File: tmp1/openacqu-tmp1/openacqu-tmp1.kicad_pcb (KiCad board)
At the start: 4 copper layers, 45 x 36 mm, 35 parts, among them J1 GSB1C41110SSHR, J2 Test Points, U1 MCP2221AT-I_ML, U2 LP5817DRLR, U3 FXL6408UMX, U4 24AA025E48T-E_OT, U5 AP2112K-3.3TRG1, U6 TPS22996HQDYCRQ1

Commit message: Added sensor to tmp1
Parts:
- added J3: SJ-3524-SMT, openacqu_footprints:CUI_SJ-3524-SMT, F.Cu at (111.9, 75.0)
- added U7: MCP9600T-E_MX, openacqu_footprints:QFN65P500X500X100-21N_MCP9600T-E_MX, F.Cu at (101.0, 64.2)

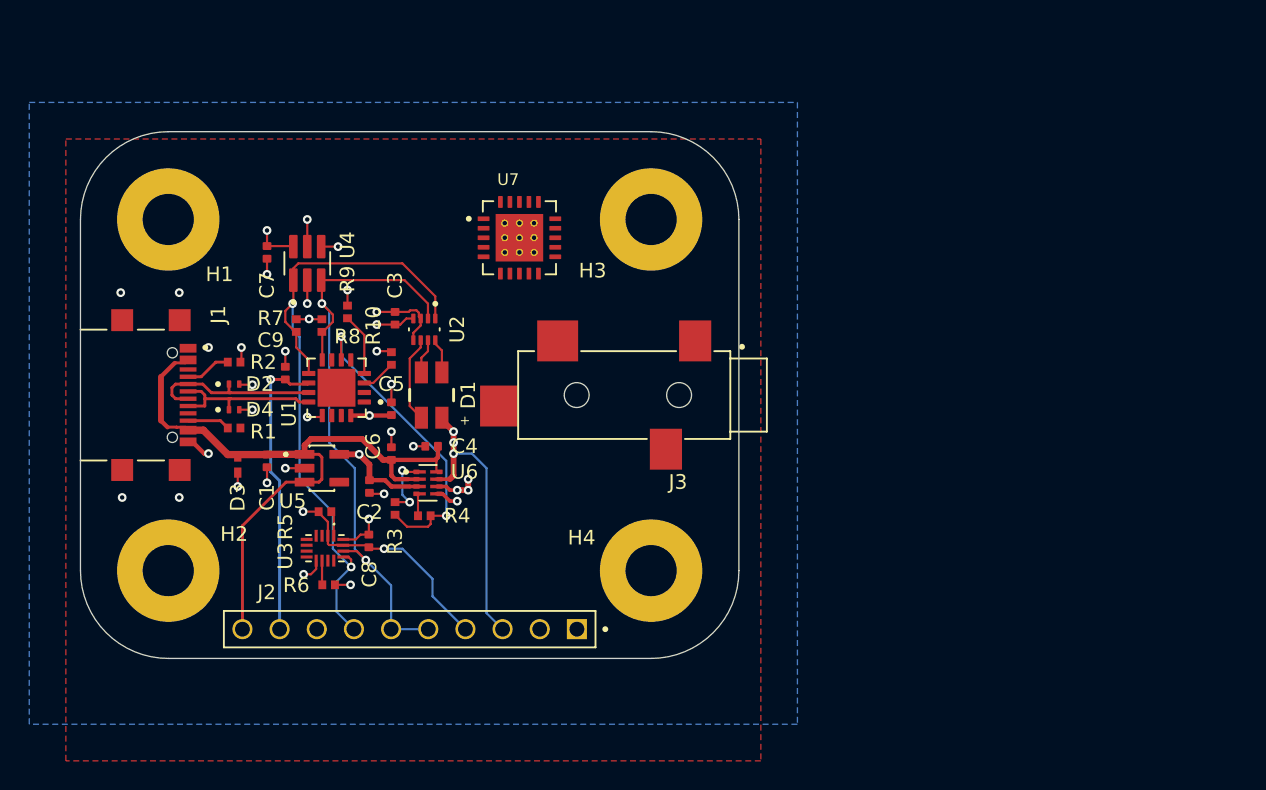
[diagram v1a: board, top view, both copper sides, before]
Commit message: Completed layout for the TMP1
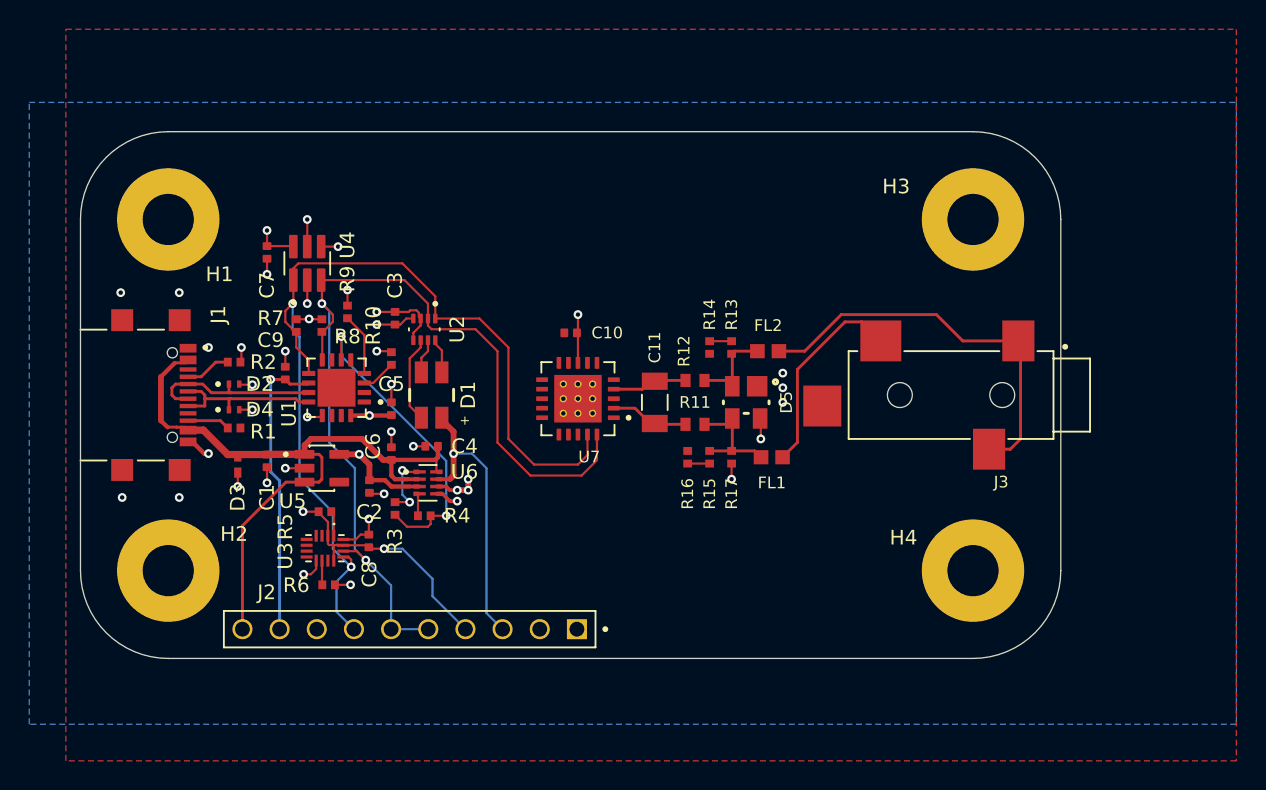
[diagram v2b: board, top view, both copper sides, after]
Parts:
- added C10: 1uF, openacqu_footprints:CAPC1005X55N, F.Cu at (104.5, 70.8)
- added C11: 100nF/50V/NPO, openacqu_footprints:CAPC3216X95N, F.Cu at (110.2, 75.5)
- added D5: 3.3V TVS, openacqu_footprints:WE-TVS_SOT143-4L, F.Cu at (116.5, 75.5)
- added FL1: 100 Ohm @ 100 MHz, openacqu_footprints:BEADC1608X65N, F.Cu at (118.2, 79.2)
- added FL2: 100 Ohm @ 100 MHz, openacqu_footprints:BEADC1608X65N, F.Cu at (118.0, 72.0)
- added R11: 100, openacqu_footprints:RESC1005X40, F.Cu at (113.0, 77.0)
- added R12: 100, openacqu_footprints:RESC1005X40, F.Cu at (113.0, 74.0)
- added R13: 1M, openacqu_footprints:RESC1005X40N, F.Cu at (115.5, 71.8)
- added R14: 1M, openacqu_footprints:RESC1005X40N, F.Cu at (114.0, 71.8)
- added R15: 1M, openacqu_footprints:RESC1005X40N, F.Cu at (114.0, 79.2)
- added R16: 1M, openacqu_footprints:RESC1005X40N, F.Cu at (112.5, 79.2)
- added R17: 1M, openacqu_footprints:RESC1005X40N, F.Cu at (115.5, 79.2)
- moved J3 22.1 mm to (134.0, 75.0)
- moved H3 22.0 mm to (132.0, 63.0)
- moved H4 22.0 mm to (132.0, 87.0)
- moved U7 11.7 mm to (105.0, 75.2), turned to 180 degrees
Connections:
- J3 pad 1: unconnected-(J3-Pad1) -> /Temp_sensor/TC_CON_N
- J3 pad 2: unconnected-(J3-Pad2) -> /Temp_sensor/TC_CON_P
- J3 pad 3: unconnected-(J3-Pad3) -> /Temp_sensor/TC_CON_N
- U3 pad 12: unconnected-(U3-GPIO0-Pad12) -> +3V3_SYS
- U7 pad 16: unconnected-(U7-ADDR-Pad16) -> GND
- U7 pad 19: unconnected-(U7-SCL-Pad19) -> /Core/SCL
- U7 pad 2: unconnected-(U7-VIN+-Pad2) -> /Temp_sensor/TC_P
- U7 pad 20: unconnected-(U7-SDA-Pad20) -> /Core/SDA
- U7 pad 21: EXP -> GND
- U7 pad 22: EXP -> GND
- U7 pad 23: EXP -> GND
- U7 pad 24: EXP -> GND
- U7 pad 25: EXP -> GND
- U7 pad 26: EXP -> GND
- U7 pad 27: EXP -> GND
- U7 pad 28: EXP -> GND
- U7 pad 29: EXP -> GND
- U7 pad 30: EXP -> GND
- U7 pad 4: unconnected-(U7-VIN--Pad4) -> /Temp_sensor/TC_N
- U7 pad 8: unconnected-(U7-VDD-Pad8) -> +3V3_SYS
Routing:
- net /Temp_sensor/TC_CON_N: track 0.00 -> 27.3 mm
- net /Core/SDA: track 43.7 -> 65.8 mm
- net /Core/SCL: track 46.3 -> 66.2 mm
- net /Temp_sensor/TC_CON_P: track 0.00 -> 14.0 mm
- net /Temp_sensor/TC_TVS_P: track 0.00 -> 8.00 mm
- net +3V3_SYS: track 27.6 -> 34.5 mm, vias 9 -> 12
- net /Temp_sensor/TC_TVS_N: track 0.00 -> 6.14 mm
- net /Temp_sensor/TC_P: track 0.00 -> 5.36 mm
- net /Temp_sensor/TC_N: track 0.00 -> 5.15 mm
- net Net-(R15-Pad2): track 0.00 -> 1.50 mm
- net Net-(R13-Pad2): track 0.00 -> 1.50 mm
- net GND: vias 27 -> 30
- net +5V0_SYS: vias 3 -> 1
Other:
- board size 45 x 36 mm -> 67 x 36 mm

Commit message: Added stitcing vias
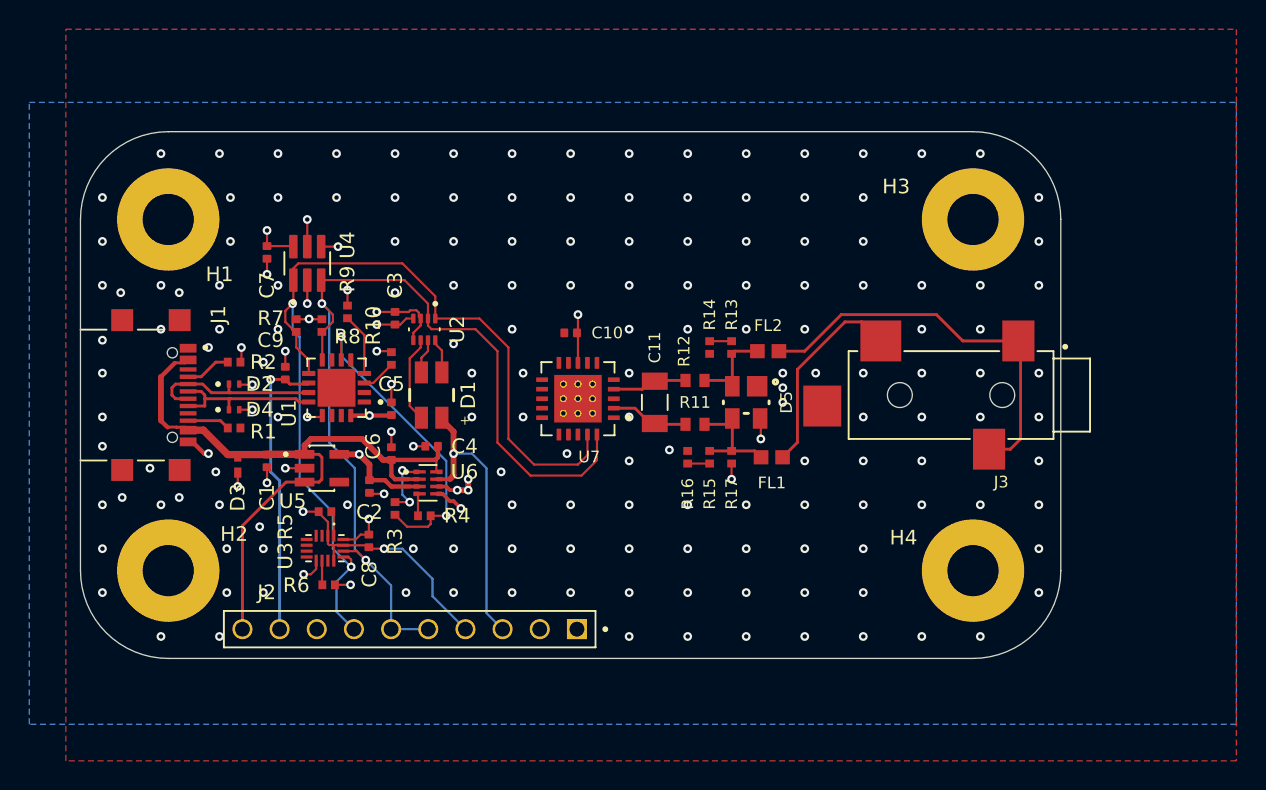
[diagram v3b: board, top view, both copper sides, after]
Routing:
- net GND: track 32.0 -> 32.5 mm, vias 30 -> 179

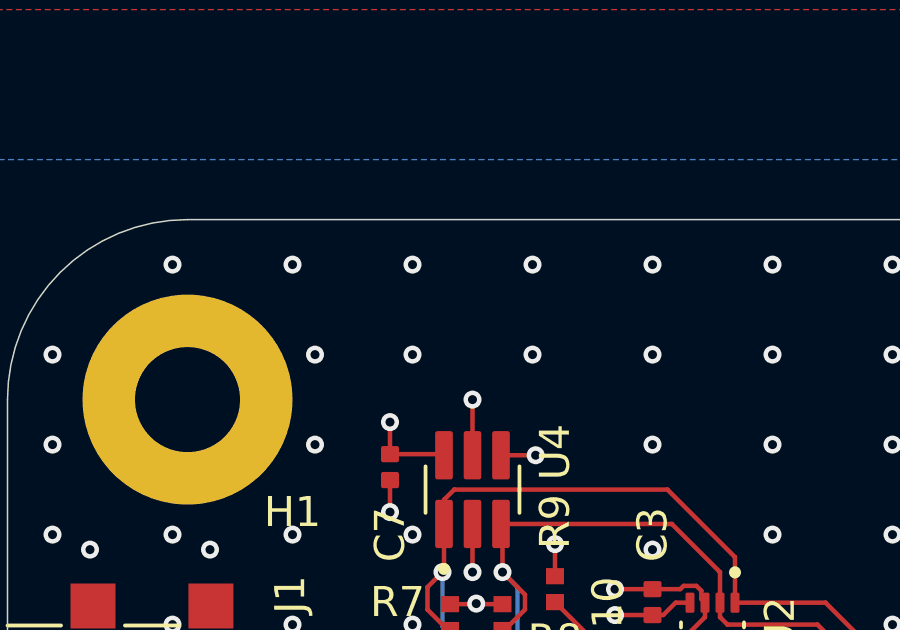
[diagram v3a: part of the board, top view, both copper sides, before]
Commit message: Updated symbols with JLCPCB part numbers
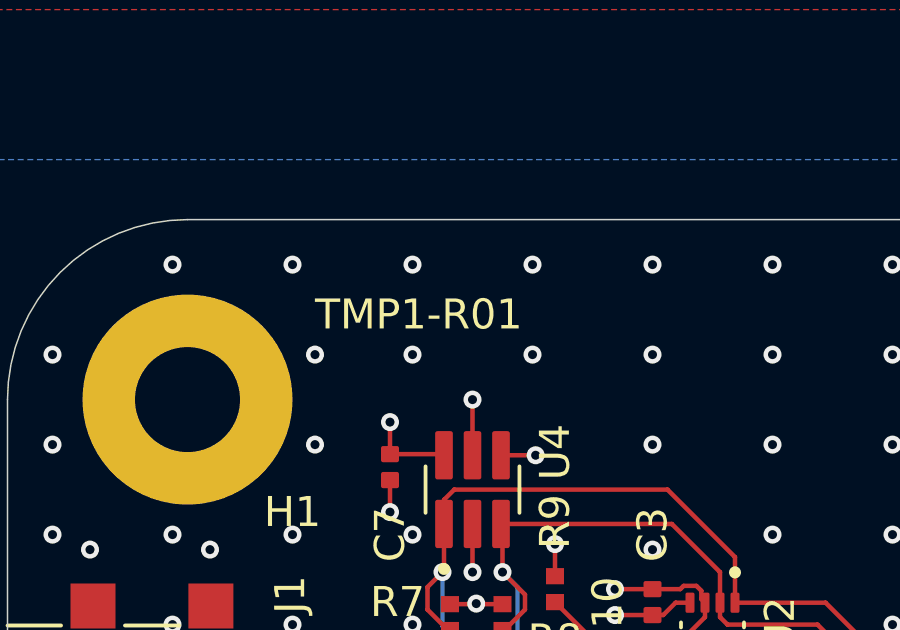
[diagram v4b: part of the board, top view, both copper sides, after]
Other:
- board text added: "TMP1-R01"
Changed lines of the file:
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@@
 		(layer "Edge.Cuts")
+	)
+	(gr_text "TMP1-R01"
+		(at 81.25 60.75 0)
+		(layer "F.SilkS")
+		(effects
+			(font
+				(size 1 1)
+				(thickness 0.1)
+			)
+			(justify left bottom)
+		)
 	)
 	(segment
